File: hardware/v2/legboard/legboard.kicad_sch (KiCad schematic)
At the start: 17 parts, among them J1 UPLINK_RJ11, J2 COXA, J3 FEMUR, J4 TIBIA, J5 SERVO_PWR_IN, U1 XIAO-RP2040, U2 SP3485CN, U3 INA4181A3IPWR

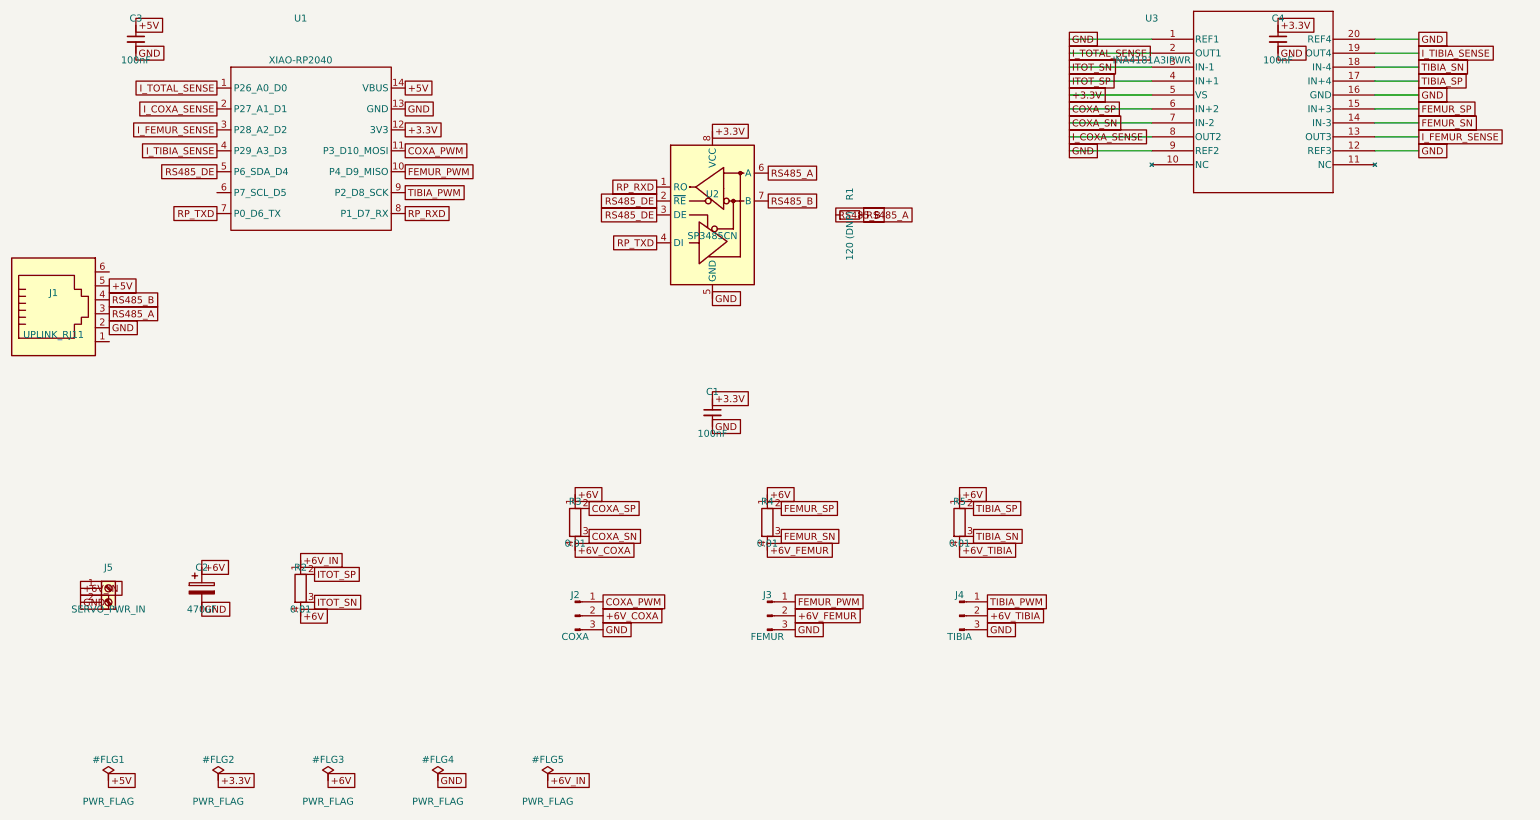
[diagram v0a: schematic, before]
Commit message: legboard sensing corrections and shunt remapping
- Fix INA4181A3IPWR gain: was 3 (copy-paste error), correct value is 100
  per datasheet (A3 suffix = gain 100); V_TO_A scale was ~33x too high
- Remap shunt resistors for better PCB layout: R4=total, R5=coxa,
  R3=femur, R2=tibia (was R2=total, R3=coxa, R4=femur, R5=tibia)
- Update ADC pin assignments on XIAO to match new shunt layout:
  A0=total, A1=femur, A2=tibia, A3=coxa
- Add leg firmware test sketch (tibia servo sweep + current readout)
  targeting XIAO RP2040 via PlatformIO; kept for v2 board validation

Co-Authored-By: Claude Sonnet 4.6 <noreply@anthropic.com>
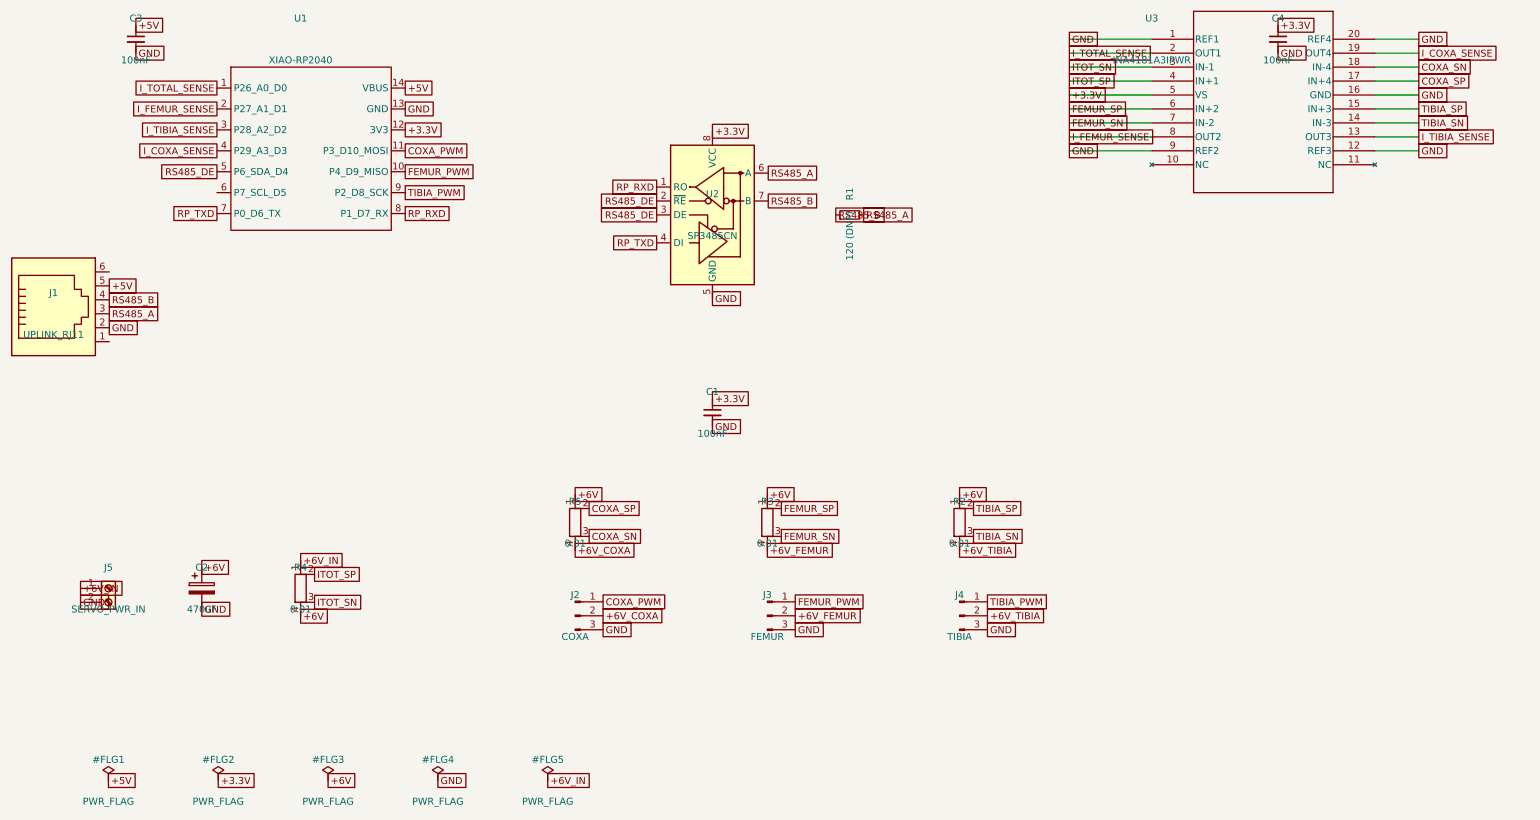
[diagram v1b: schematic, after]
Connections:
- net +6V: now also R2.1, R4.4; no longer R2.4, R4.1
- net +6V_COXA: now also R5.4; no longer R3.4
- net +6V_FEMUR: now also R3.4; no longer R4.4
- net +6V_IN: now also R4.1; no longer R2.1
- net +6V_TIBIA: now also R2.4; no longer R5.4
- net COXA_SN: now also R5.3, U3.18 (IN-4); no longer R3.3, U3.7 (IN-2)
- net COXA_SP: now also R5.2, U3.17 (IN+4); no longer R3.2, U3.6 (IN+2)
- net FEMUR_SN: now also R3.3, U3.7 (IN-2); no longer R4.3, U3.14 (IN-3)
- net FEMUR_SP: now also R3.2, U3.6 (IN+2); no longer R4.2, U3.15 (IN+3)
- net ITOT_SN: now also R4.3; no longer R2.3
- net ITOT_SP: now also R4.2; no longer R2.2
- net I_COXA_SENSE: now also U1.4 (P29_A3_D3), U3.19 (OUT4); no longer U1.2 (P27_A1_D1), U3.8 (OUT2)
- net I_FEMUR_SENSE: now also U1.2 (P27_A1_D1), U3.8 (OUT2); no longer U1.3 (P28_A2_D2), U3.13 (OUT3)
- net I_TIBIA_SENSE: now also U1.3 (P28_A2_D2), U3.13 (OUT3); no longer U1.4 (P29_A3_D3), U3.19 (OUT4)
- net TIBIA_SN: now also R2.3, U3.14 (IN-3); no longer R5.3, U3.18 (IN-4)
- net TIBIA_SP: now also R2.2, U3.15 (IN+3); no longer R5.2, U3.17 (IN+4)
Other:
- moved on the sheet: R2, R3, R4, R5
